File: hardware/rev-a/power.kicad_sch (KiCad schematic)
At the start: 16 parts, among them U1 BQ24074RGT, U2 TLV75533PDBV

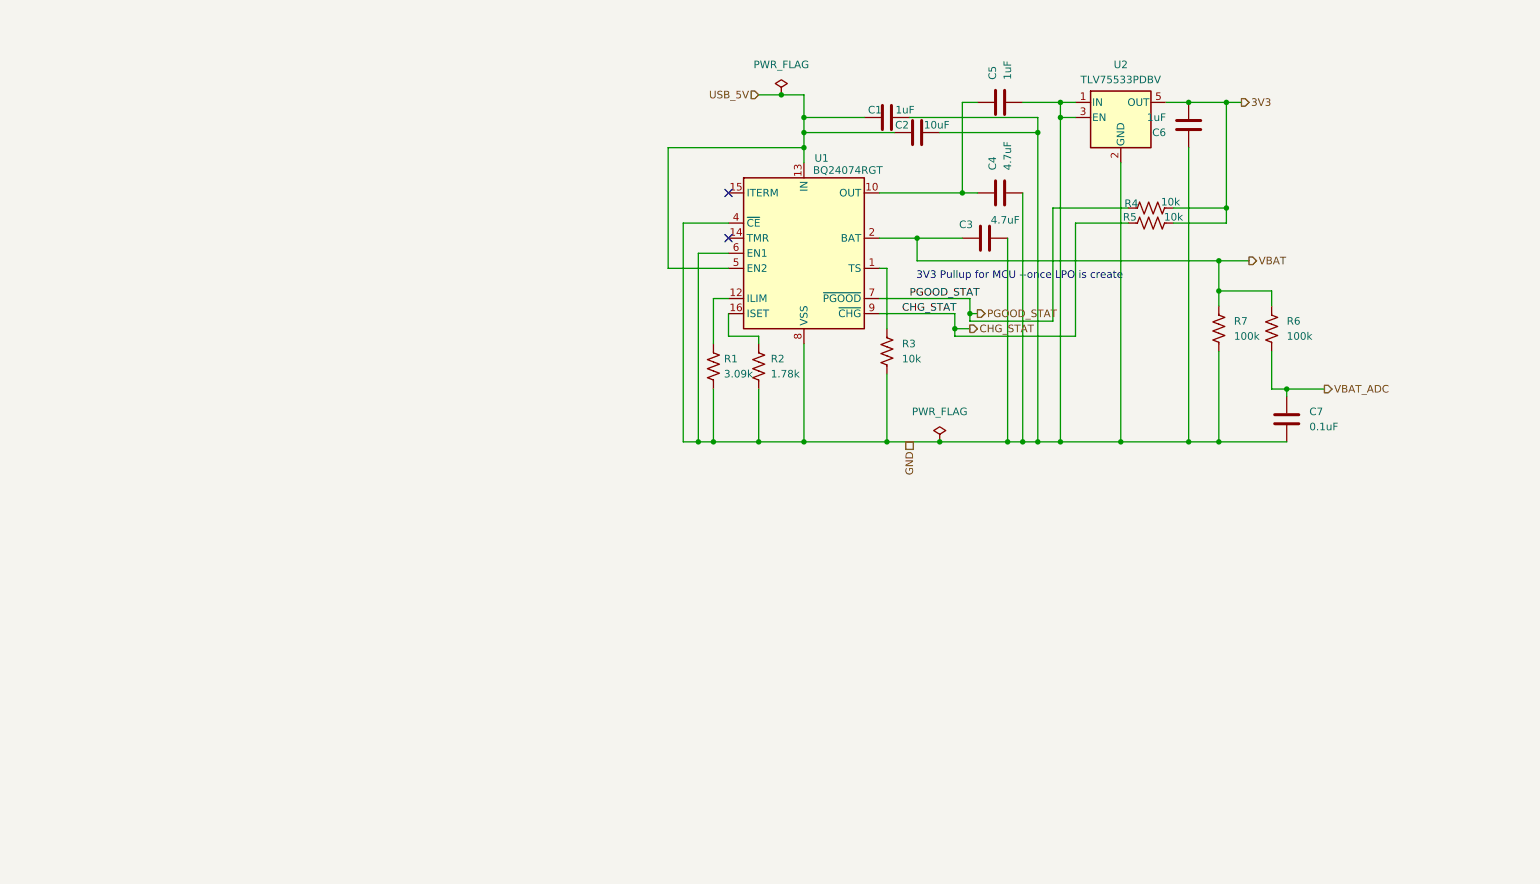
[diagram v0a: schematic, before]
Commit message: finalize MCU sheet and add haptic feedback sheet
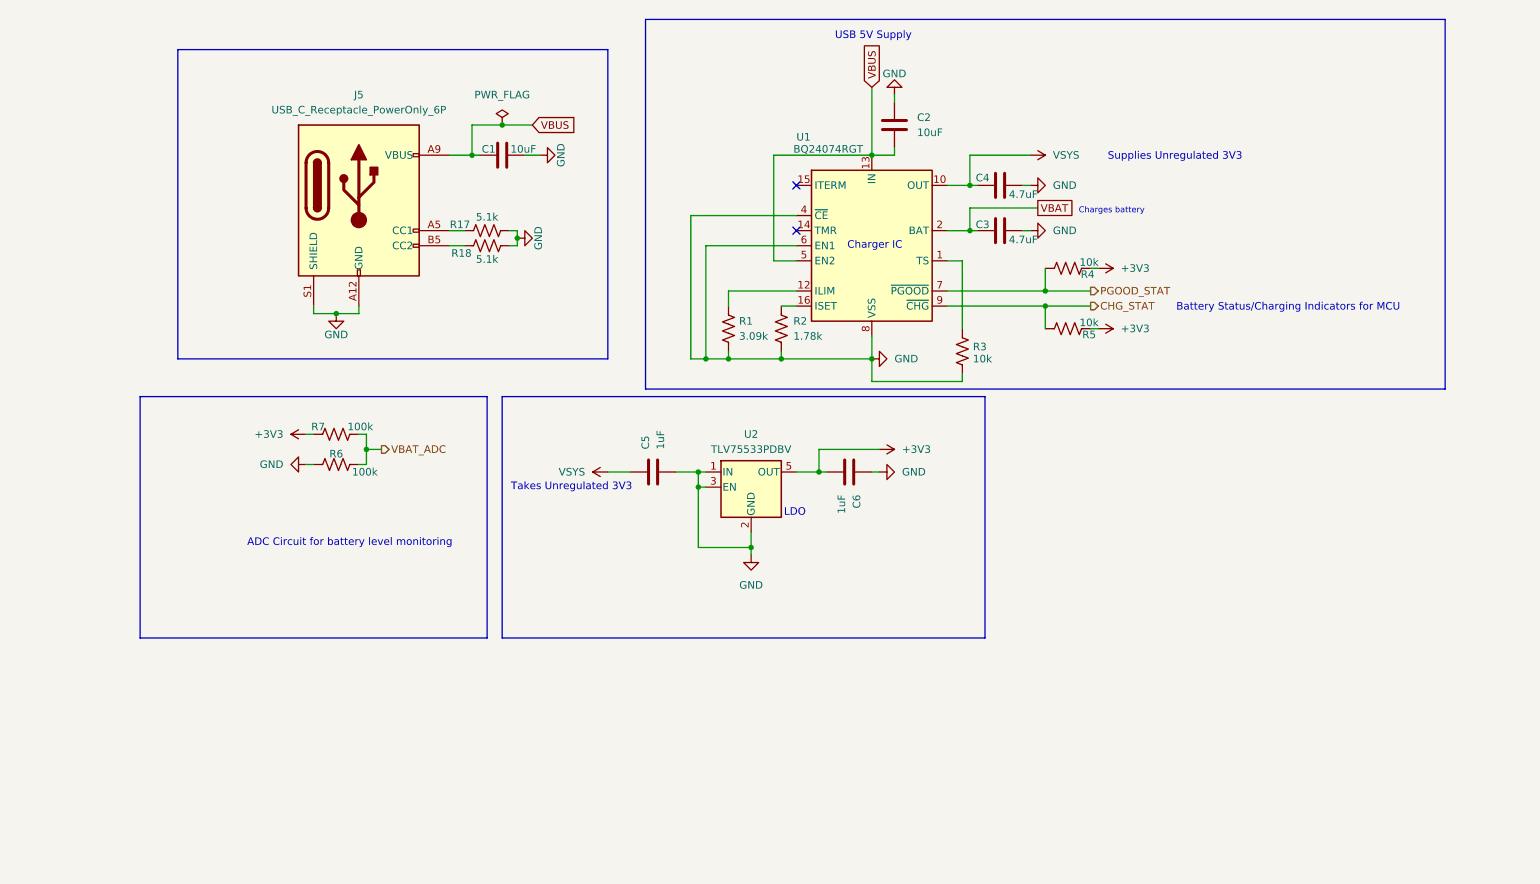
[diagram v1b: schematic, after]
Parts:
- removed C7: 0.1uF, symbol Device:C
- added J5: USB_C_Receptacle_PowerOnly_6P, symbol Connector:USB_C_Receptacle_PowerOnly_6P
- added R17, R18: 5.1k, symbol Device:R_US
- C1: value 1uF -> 10uF
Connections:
- net CHG_STAT: now also R5.2; no longer R5.1
- net GND: now also R6.1, J5.A12 (GND), J5.B12 (GND), J5.S1 (SHIELD), R17.2, R18.2; no longer R7.2
- net PGOOD_STAT: now also R4.2; no longer R4.1
- net VBAT: no longer R6.1, R7.1
- net VBAT_ADC: now also R7.2
- net VSYS: now reaches C4.1, C5.1, U1.10 (OUT), U1.11 (OUT)
- net 3V3 renamed +3V3
- net +3V3: now also R4.1, R5.1, R7.1; no longer R4.2, R5.2
- net USB_5V renamed VBUS
- net VBUS: now also J5.A9 (VBUS), J5.B9 (VBUS)
- new net: J5.A5 (CC1), R17.1
- new net: J5.B5 (CC2), R18.1
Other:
- note added: "ADC Circuit for battery level monitoring"
- note added: "Battery Status/Charging Indicators for MCU"
- note added: "Charger IC"
- note added: "Charges battery"
- note added: "LDO"
- note added: "Supplies Unregulated 3V3"
- note added: "Takes Unregulated 3V3"
- note added: "USB 5V Supply"
- note removed: "3V3 Pullup for MCU --once LPO is create"
- title: (none) -> power sheet
- moved on the sheet: C2, C3, C4, C5, C6, R1, R2, R3, R4, R5, R6, R7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

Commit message: Annotate schematic hierarchy and fix LED routing
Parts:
- added J2: Conn_01x02, symbol Connector_Generic:Conn_01x02
- added TP1: TestPoint, symbol Connector:TestPoint
- R5: renamed from R1; value 3.09k -> 3k
- R6: renamed from R2; value 1.78k -> 1.8k
- renumbered C5 to C2, C6 to C3, C2 to C4, C4 to C5, C3 to C6, J5 to J1, R7 to R1, R6 to R2, R17 to R3, R18 to R4, R3 to R7, R4 to R8, R5 to R9
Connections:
- net GND: now also C1.1, J2.2 (Pin_2); no longer C1.2
- net VBAT: now also J2.1 (Pin_1), TP1.1
- net VBUS: now also C1.2; no longer C1.1
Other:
- note added: "Unregulated Rail"
- note added: "battery"
- note removed: "Charges battery"
- note removed: "Takes Unregulated 3V3"
- moved on the sheet: C1, R1, R2

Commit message: rev: schematic revision B
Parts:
- C1, C2, C3, C4, C5, C6: footprint (none) -> Capacitor_SMD:C_0603_1608Metric
- J1: footprint (none) -> Connector_USB:USB_C_Receptacle_HRO_TYPE-C-31-M-12
- J2: footprint (none) -> Connector_JST:JST_PH_B2B-PH-K_1x02_P2.00mm_Vertical
- R1, R2, R3, R4, R5, R6, R7, R8, R9: footprint (none) -> Resistor_SMD:R_0603_1608Metric
- TP1: footprint (none) -> TestPoint:TestPoint_Pad_D1.0mm
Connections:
- net +3V3: no longer R1.1
- net VBAT: now also R1.1

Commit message: intialize PCB layout document
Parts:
- added R24: 10K, symbol Device:R_US
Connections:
- net +3V3: now also C3.1; no longer C3.2
- net GND: now also C2.1, C3.2; no longer C2.2, C3.1, U2.1 (IN), U2.3 (EN)
- net VBUS: now also R24.1; no longer U1.5 (EN2)
- net VSYS: now also C2.2, U2.1 (IN), U2.3 (EN); no longer C2.1
- new net: R24.2, U1.5 (EN2)
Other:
- note added: "3.7V"
- note added: "JST-PH for LiPo Battery"
- note added: "USBC Receptacle -- For Power"
- note removed: "Unregulated Rail"
- moved on the sheet: C2, C3, R7

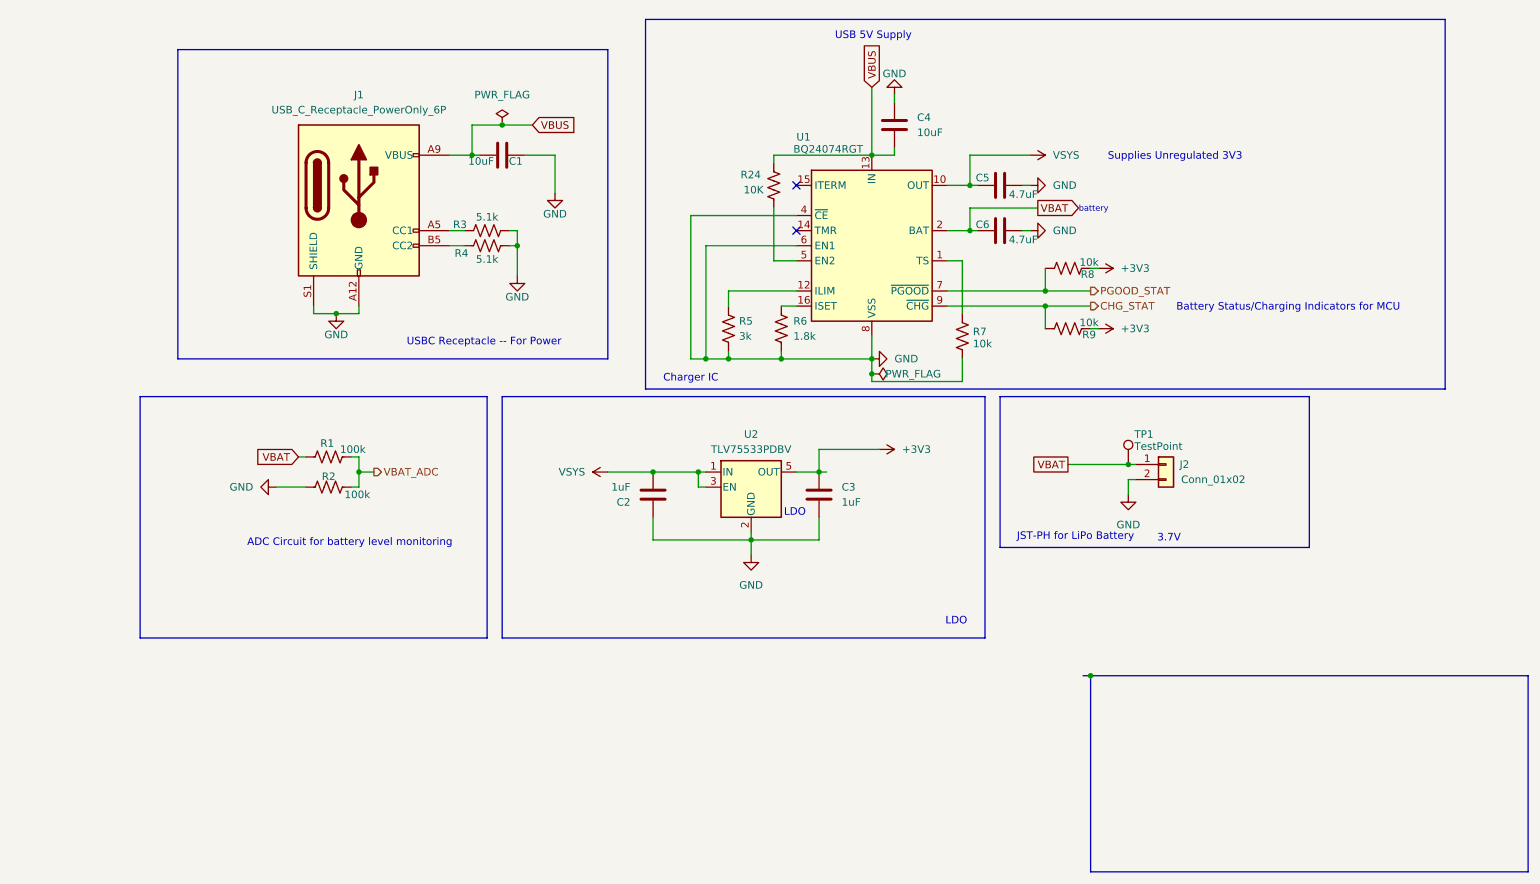
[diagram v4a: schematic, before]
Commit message: Assign footprints and add additional bypass caps
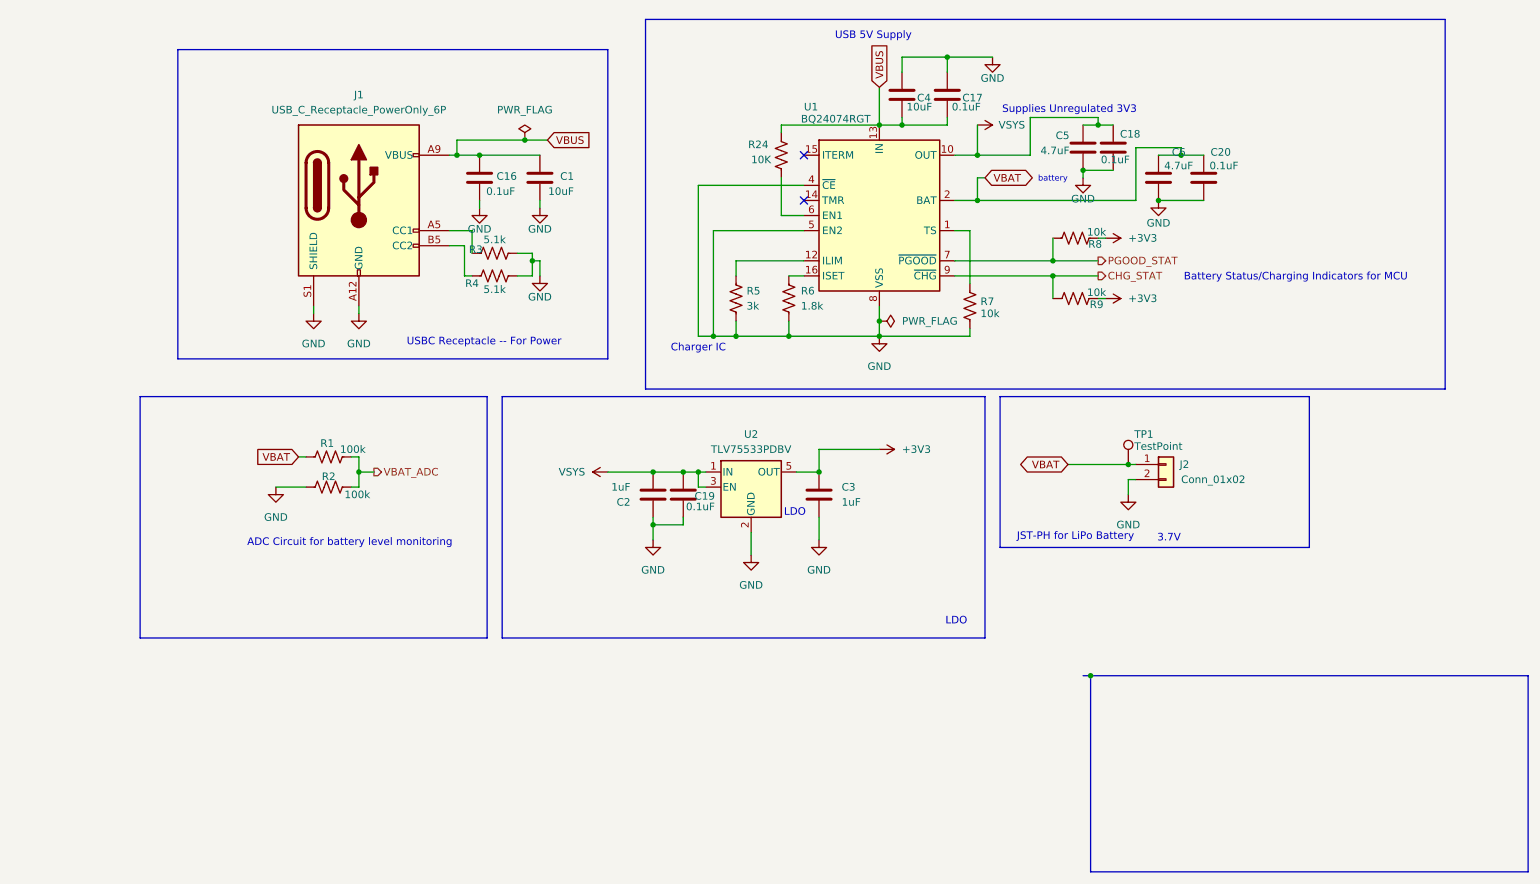
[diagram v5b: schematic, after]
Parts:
- added C16, C17, C18, C19, C20: 0.1uF, Capacitor_SMD:C_0603_1608Metric, symbol Device:C
- J1: footprint Connector_USB:USB_C_Receptacle_HRO_TYPE-C-31-M-12 -> USB4105-GF-A:GCT_USB4105-GF-A
- R24: footprint (none) -> Resistor_SMD:R_0603_1608Metric
- U1: footprint Package_DFN_QFN:VQFN-16-1EP_3x3mm_P0.5mm_EP1.6x1.6mm -> BQ24074RGTRG4:QFN50P300X300X100-17N
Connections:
- net GND: now also C1.2, C5.1, C6.1, U1.5 (EN2), C16.2, C17.2, C18.1, C19.1, C20.1; no longer C1.1, C5.2, C6.2, U1.6 (EN1)
- net VBAT: now also C6.2, C20.2; no longer C6.1
- net VBUS: now also C1.1, C16.1, C17.1; no longer C1.2
- net VSYS: now also C5.2, C18.2, C19.2; no longer C5.1
- net at R24.2: now also U1.6 (EN1); no longer U1.5 (EN2)
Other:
- moved on the sheet: C1, C4, C5, C6, R24, R3, R4, R5, R6, R7, R8, R9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

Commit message: updated layout from schematic
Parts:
- J1: footprint USB4105-GF-A:GCT_USB4105-GF-A -> Connector_USB:USB_C_Receptacle_GCT_USB4105-xx-A_16P_TopMnt_Horizontal
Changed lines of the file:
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@@
 			)
 		)
-		(property "Footprint" "USB4105-GF-A:GCT_USB4105-GF-A"
+		(property "Footprint" "Connector_USB:USB_C_Receptacle_GCT_USB4105-xx-A_16P_TopMnt_Horizontal"
 			(at 74.93 41.91 0)
 			(effects

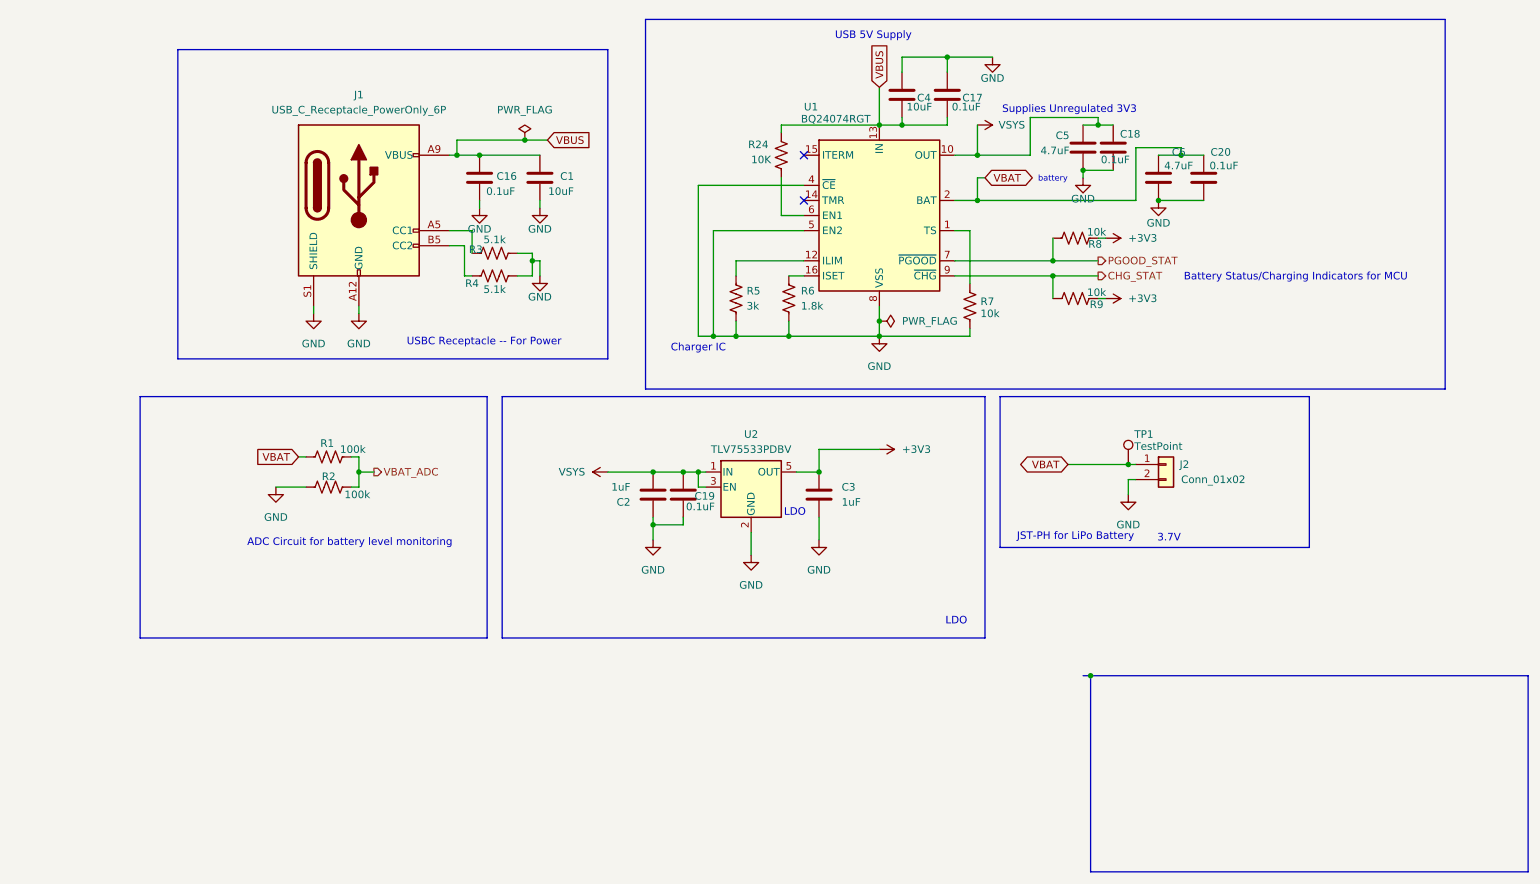
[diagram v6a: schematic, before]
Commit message: format schematic to fit convention, replace SWD header with 2x5
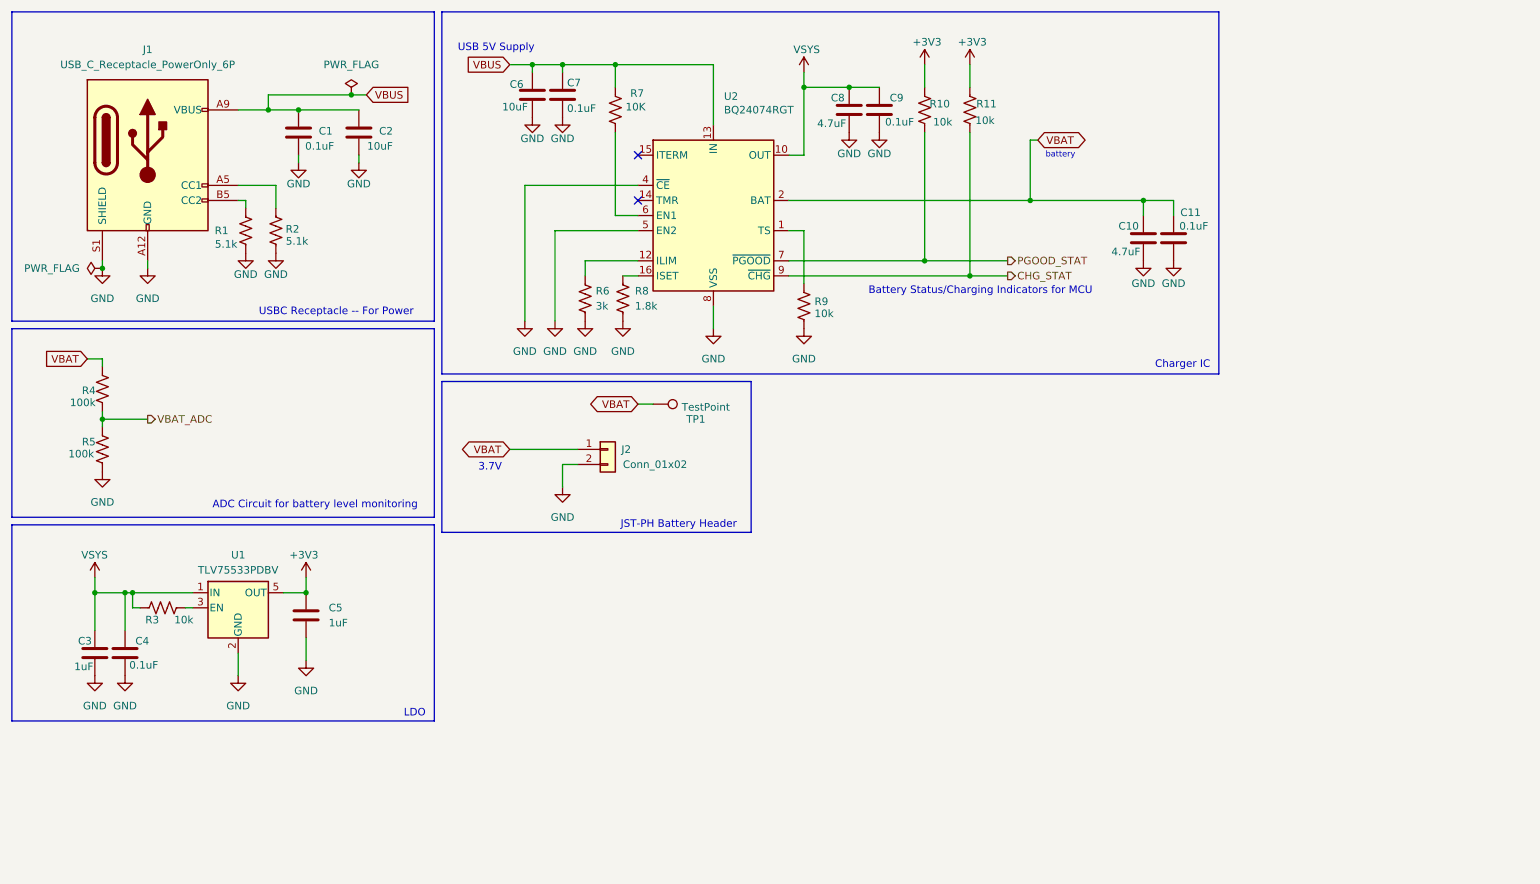
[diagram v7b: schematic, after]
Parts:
- added R3: 10k, Resistor_SMD:R_0603_1608Metric, symbol Device:R_US
- renumbered C16 to C1, C6 to C10, C20 to C11, C1 to C2, C2 to C3, C19 to C4, C3 to C5, C4 to C6, C17 to C7, C5 to C8, C18 to C9, R4 to R1, R8 to R10, R9 to R11, R3 to R2, R1 to R4, R2 to R5, R5 to R6, R24 to R7, R6 to R8, R7 to R9, U2 to U1, U1 to U2
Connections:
- net +3V3: now also R10.2; no longer R10.1
- net GND: now also C6.1, C7.1, R2.1; no longer C6.2, C7.2, R2.2
- net PGOOD_STAT: now also R10.1; no longer R10.2
- net VBAT: now also R4.2; no longer R4.1
- net VBAT_ADC: now also R4.1; no longer R4.2
- net VBUS: now also C6.2, C7.2, R7.2; no longer C6.1, C7.1, R7.1
- net VSYS: now also R3.1; no longer U1.3 (EN)
- net at J1.A5 (CC1): now also R2.2; no longer R2.1
- net at U2.6 (EN1): now also R7.1; no longer R7.2
- new net: R3.2, U1.3 (EN)
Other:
- note added: "JST-PH Battery Header"
- note removed: "JST-PH for LiPo Battery"
- note removed: "Supplies Unregulated 3V3"
- moved on the sheet: C1, C10, C11, C2, C3, C4, C5, C6, C7, C8, C9, J1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
